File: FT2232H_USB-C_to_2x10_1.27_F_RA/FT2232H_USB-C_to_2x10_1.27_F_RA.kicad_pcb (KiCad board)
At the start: 4 copper layers, 43 x 60 mm, 44 parts, among them J1 USB_C_USB2.0, J2 Conn_02x10_Odd_Even, J3 Conn_02x10_Odd_Even, U1 FT2232HL, U2 93C46BT-I_OT, U3 USBLC6-2SC6, U4 MIC5504-3.3YM5, X1 DSC60xx

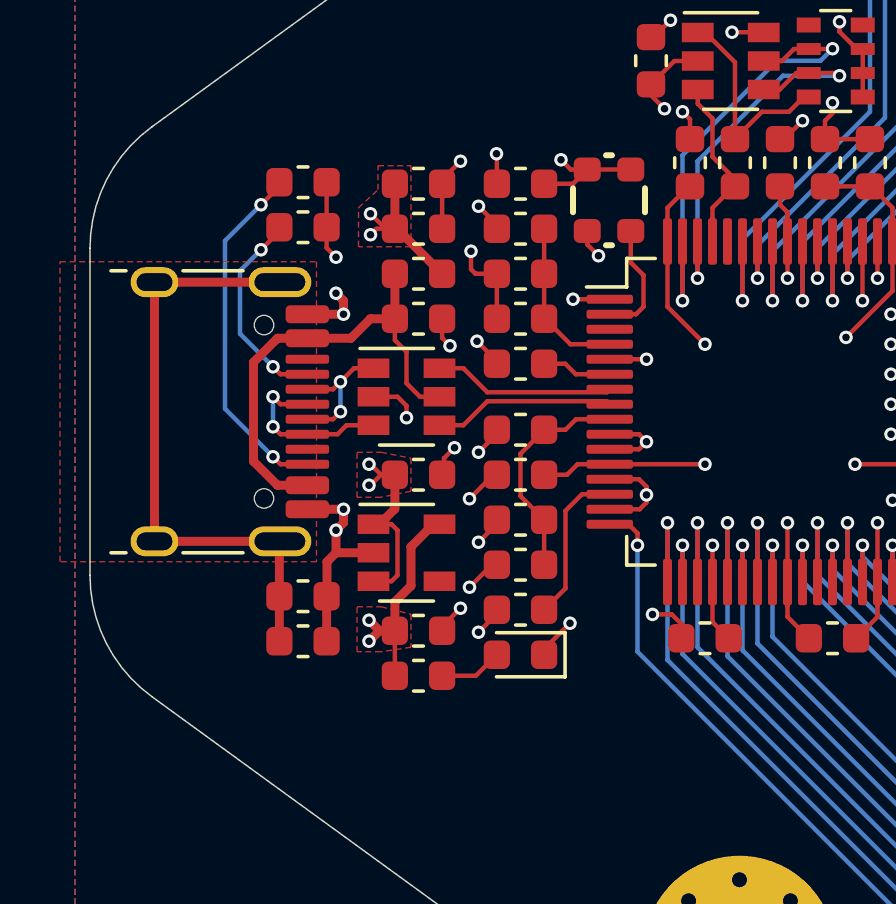
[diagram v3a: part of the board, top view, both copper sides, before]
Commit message: Implement option to use LDO with bypass capacitor
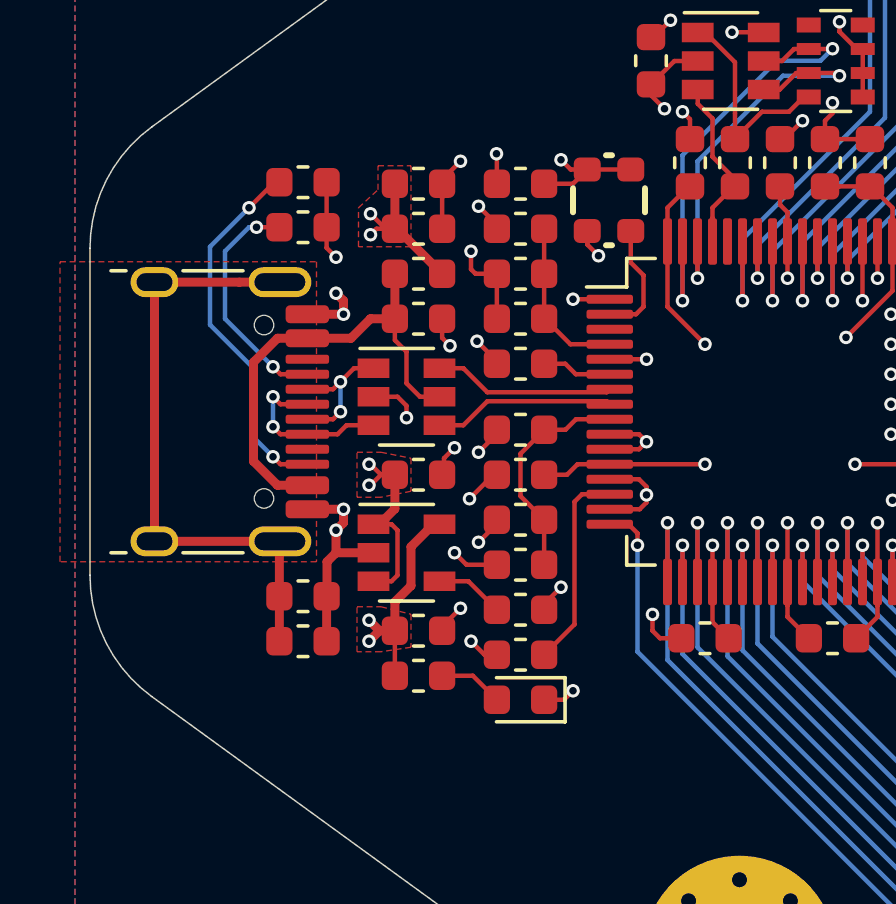
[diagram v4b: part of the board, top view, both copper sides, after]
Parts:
- added C22: 10n, Capacitor_SMD:C_0603_1608Metric, F.Cu at (152.3, 103.6)
- U4: value MIC5504-3.3YM5 -> LDO_SOT-23-5
- moved D1 1.50 mm to (152.3, 106.6)
- moved R2 1.50 mm to (152.3, 105.1)
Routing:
- net Net-(C22-Pad1): track 0.00 -> 2.31 mm
- net Net-(R2-Pad1): track 5.30 -> 6.80 mm
- net /USB_CC1: track 6.90 -> 7.91 mm
- net USB_5V: track 102.9 -> 103.6 mm
- net GND: track 61.3 -> 62.0 mm, vias 31 -> 32
- net /USB_CC2: track 11.8 -> 12.3 mm

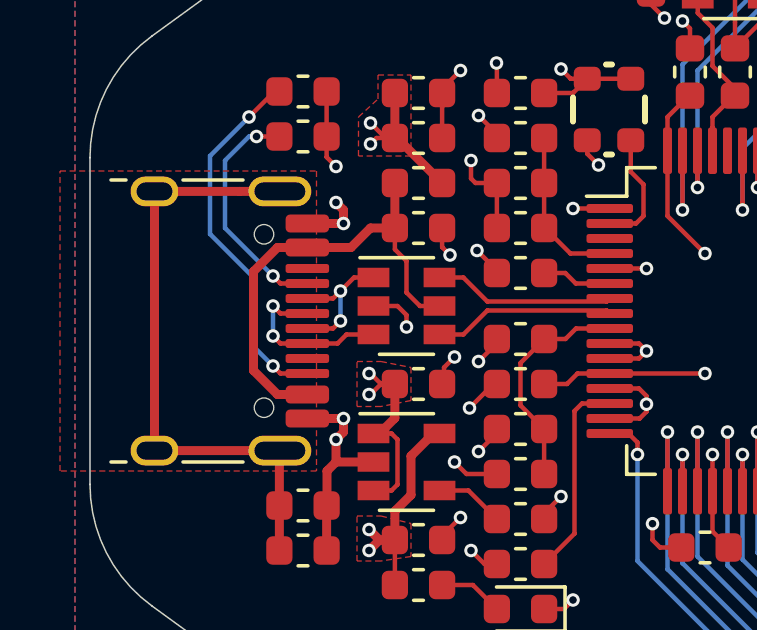
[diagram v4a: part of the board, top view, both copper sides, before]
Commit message: Simplify routing of USB 2.0 data lines
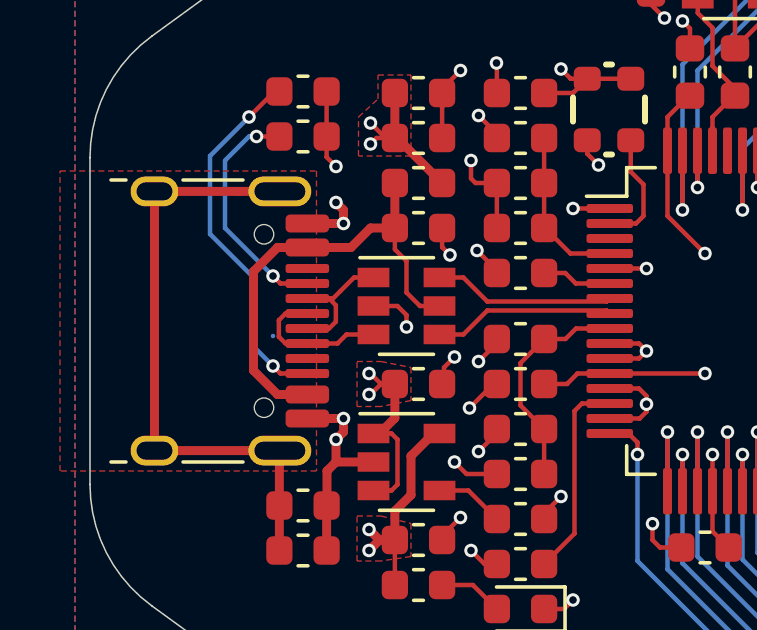
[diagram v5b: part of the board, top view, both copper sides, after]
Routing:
- net /xUSB_D+: track 5.83 -> 4.97 mm, vias 2 -> 0
- net /xUSB_D-: track 4.70 -> 5.13 mm, vias 2 -> 0
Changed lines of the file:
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@@
     (thickness 1.2)
     (drawings 63)
-    (tracks 621)
+    (tracks 619)
     (zones 0)
     (modules 45)
@@
   (segment (start 146.25 97.778) (end 146.55 97.478) (width 0.15) (layer F.Cu) (net 10))
   (segment (start 145.245 97.778) (end 146.25 97.778) (width 0.15) (layer F.Cu) (net 10))
-  (segment (start 145.245 97.778) (end 144.349998 97.778) (width 0.15) (layer F.Cu) (net 10))
-  (via (at 144.099998 97.528) (size 0.45) (drill 0.25) (layers F.Cu B.Cu) (net 10))
-  (segment (start 144.349998 97.778) (end 144.099998 97.528) (width 0.15) (layer F.Cu) (net 10))
   (segment (start 144.099998 97.528) (end 144.1 97.527998) (width 0.15) (layer B.Cu) (net 10))
-  (segment (start 144.35 96.778) (end 144.1 96.528) (width 0.15) (layer F.Cu) (net 10))
-  (segment (start 144.1 97.527998) (end 144.1 96.528) (width 0.15) (layer B.Cu) (net 10))
-  (segment (start 145.245 96.778) (end 144.35 96.778) (width 0.15) (layer F.Cu) (net 10))
-  (via (at 144.1 96.528) (size 0.45) (drill 0.25) (layers F.Cu B.Cu) (net 10))
-  (segment (start 145.245 97.278) (end 146.1 97.278) (width 0.15) (layer F.Cu) (net 11))
-  (via (at 146.35 97.028) (size 0.45) (drill 0.25) (layers F.Cu B.Cu) (net 11))
-  (segment (start 146.1 97.278) (end 146.35 97.028) (width 0.15) (layer F.Cu) (net 11))
-  (segment (start 146.35 97.028) (end 146.35 96.028) (width 0.15) (layer B.Cu) (net 11))
-  (via (at 146.35 96.028) (size 0.45) (drill 0.25) (layers F.Cu B.Cu) (net 11))
+  (segment (start 144.52 96.778) (end 145.245 96.778) (width 0.15) (layer F.Cu) (net 10))
+  (segment (start 144.29499 97.00301) (end 144.52 96.778) (width 0.15) (layer F.Cu) (net 10))
+  (segment (start 144.52 97.778) (end 144.29499 97.55299) (width 0.15) (layer F.Cu) (net 10))
+  (segment (start 144.29499 97.55299) (end 144.29499 97.00301) (width 0.15) (layer F.Cu) (net 10))
+  (segment (start 145.245 97.778) (end 144.52 97.778) (width 0.15) (layer F.Cu) (net 10))
   (segment (start 146.1 96.278) (end 146.35 96.028) (width 0.15) (layer F.Cu) (net 11))
   (segment (start 145.245 96.278) (end 146.1 96.278) (width 0.15) (layer F.Cu) (net 11))
   (segment (start 147.45 95.578) (end 146.8 95.578) (width 0.15) (layer F.Cu) (net 11))
   (segment (start 146.8 95.578) (end 146.35 96.028) (width 0.15) (layer F.Cu) (net 11))
+  (segment (start 145.97 96.278) (end 145.245 96.278) (width 0.15) (layer F.Cu) (net 11))
+  (segment (start 146.19501 97.05299) (end 146.19501 96.50301) (width 0.15) (layer F.Cu) (net 11))
+  (segment (start 145.97 97.278) (end 146.19501 97.05299) (width 0.15) (layer F.Cu) (net 11))
+  (segment (start 146.19501 96.50301) (end 145.97 96.278) (width 0.15) (layer F.Cu) (net 11))
+  (segment (start 145.245 97.278) (end 145.97 97.278) (width 0.15) (layer F.Cu) (net 11))
   (via (at 164.75 99.978) (size 0.45) (drill 0.25) (layers F.Cu B.Cu) (net 12))
   (segment (start 165.25 99.978) (end 164.75 99.978) (width 0.15) (layer F.Cu) (net 12))
